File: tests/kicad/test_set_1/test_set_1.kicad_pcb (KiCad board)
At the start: 2 copper layers, 100 x 100 mm, 3 parts, among them J1 Vin, J2 Isens, J4 Conn_01x24_Socket

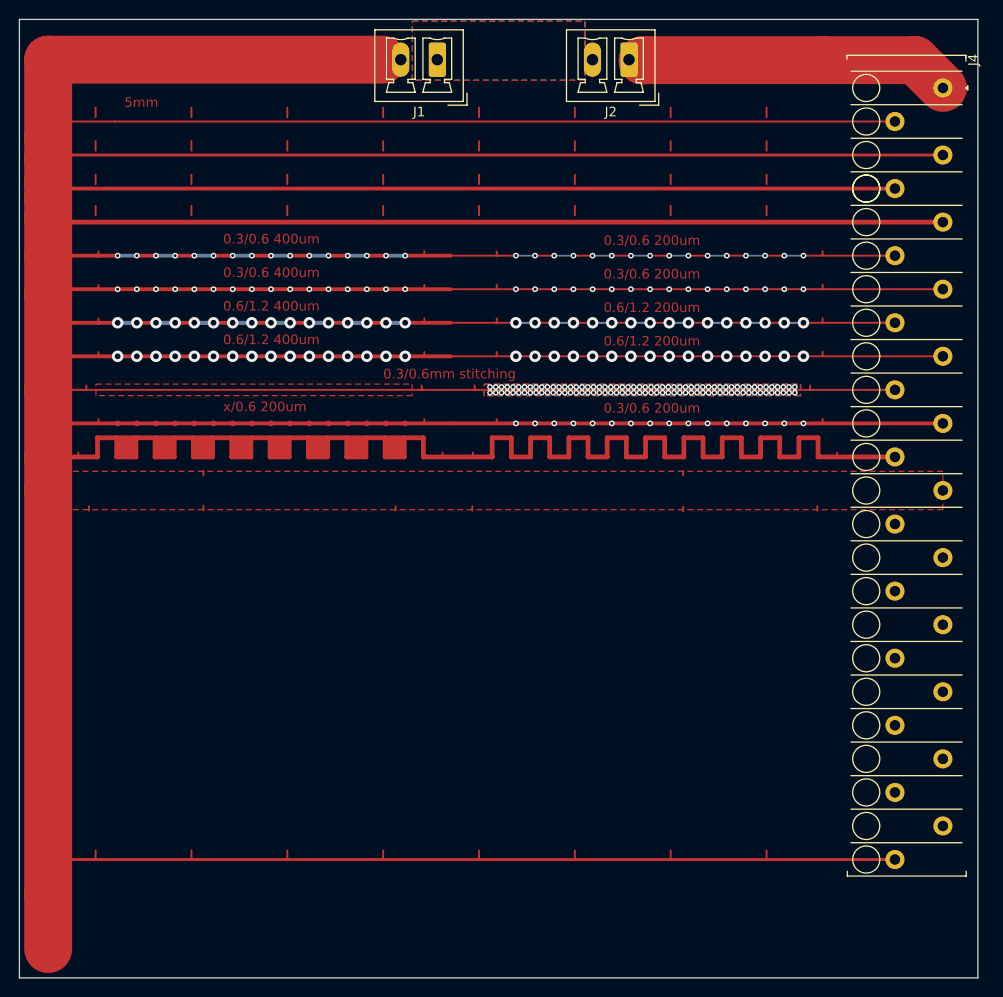
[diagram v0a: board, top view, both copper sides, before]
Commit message: test: More progress on the test_set_1 board
Add explicit test point pads to make test suite integration easier.
Also finish the "weird geometry" bunch of test cases.
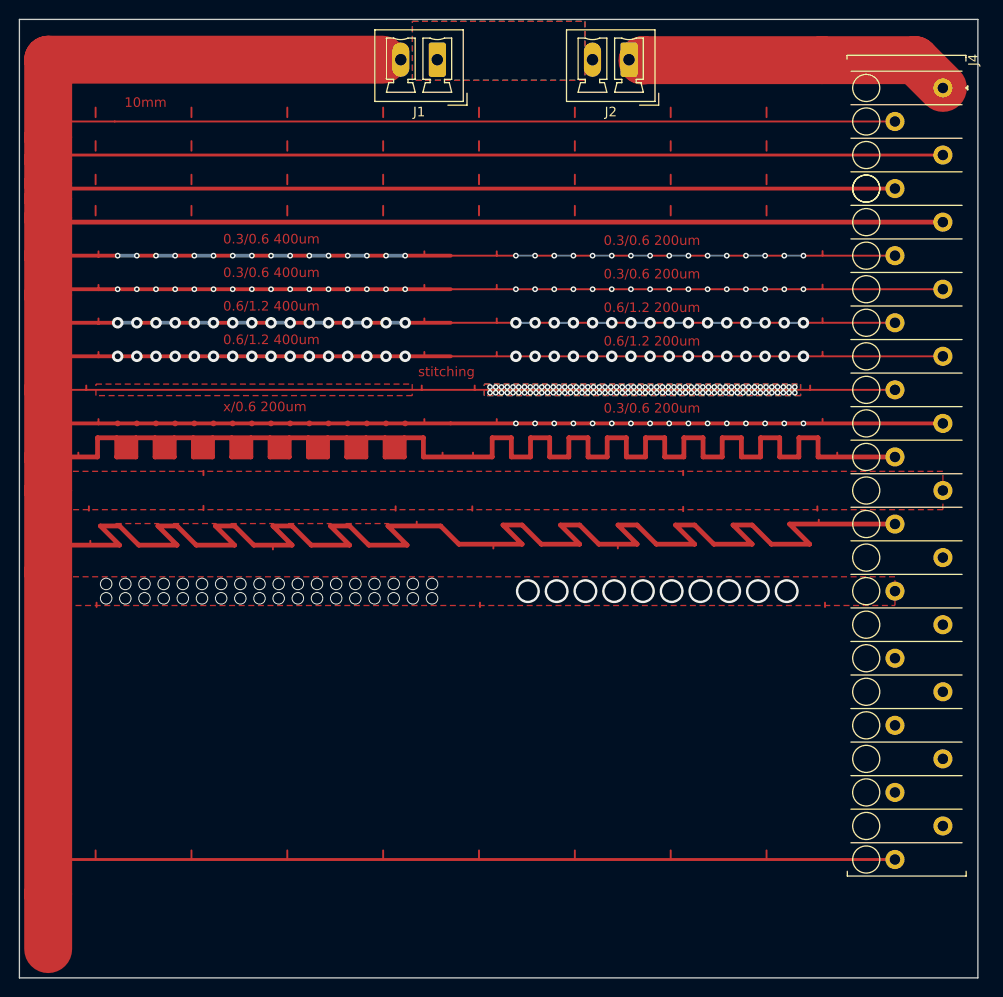
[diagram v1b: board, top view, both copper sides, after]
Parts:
- added TP1: TestPoint_Small, padne_footprints:ProbePoint, F.Cu at (107.2, 101.2)
- added TP10: TestPoint_Small, padne_footprints:ProbePoint, F.Cu at (144.2, 95.2)
- added TP11: TestPoint_Small, padne_footprints:ProbePoint, F.Cu at (147.3, 95.2)
- added TP12: TestPoint_Small, padne_footprints:ProbePoint, F.Cu at (185.3, 95.2)
- added TP13: TestPoint_Small, padne_footprints:ProbePoint, F.Cu at (108.2, 91.7)
- added TP14: TestPoint_Small, padne_footprints:ProbePoint, F.Cu at (142.2, 91.7)
- added TP15: TestPoint_Small, padne_footprints:ProbePoint, F.Cu at (149.8, 91.7)
- added TP16: TestPoint_Small, padne_footprints:ProbePoint, F.Cu at (183.8, 91.7)
- added TP17: TestPoint_Small, padne_footprints:ProbePoint, F.Cu at (107.0, 88.2)
- added TP18: TestPoint_Small, padne_footprints:ProbePoint, F.Cu at (142.0, 88.2)
- added TP19: TestPoint_Small, padne_footprints:ProbePoint, F.Cu at (147.5, 88.2)
- added TP2: TestPoint_Small, padne_footprints:ProbePoint, F.Cu at (119.2, 101.2)
- added TP20: TestPoint_Small, padne_footprints:ProbePoint, F.Cu at (182.5, 88.2)
- added TP21: TestPoint_Small, padne_footprints:ProbePoint, F.Cu at (108.2, 84.7)
- added TP22: TestPoint_Small, padne_footprints:ProbePoint, F.Cu at (142.2, 84.7)
- added TP23: TestPoint_Small, padne_footprints:ProbePoint, F.Cu at (149.8, 84.7)
- added TP24: TestPoint_Small, padne_footprints:ProbePoint, F.Cu at (183.8, 84.7)
- added TP25: TestPoint_Small, padne_footprints:ProbePoint, F.Cu at (108.2, 81.2)
- added TP26: TestPoint_Small, padne_footprints:ProbePoint, F.Cu at (142.2, 81.2)
- added TP27: TestPoint_Small, padne_footprints:ProbePoint, F.Cu at (149.8, 81.2)
- added TP28: TestPoint_Small, padne_footprints:ProbePoint, F.Cu at (183.8, 81.2)
- added TP29: TestPoint_Small, padne_footprints:ProbePoint, F.Cu at (108.2, 77.7)
- added TP3: TestPoint_Small, padne_footprints:ProbePoint, F.Cu at (119.2, 97.1)
- added TP30: TestPoint_Small, padne_footprints:ProbePoint, F.Cu at (142.2, 77.7)
- added TP31: TestPoint_Small, padne_footprints:ProbePoint, F.Cu at (149.8, 77.7)
- added TP32: TestPoint_Small, padne_footprints:ProbePoint, F.Cu at (183.8, 77.7)
- added TP33: TestPoint_Small, padne_footprints:ProbePoint, F.Cu at (108.2, 74.2)
- added TP34: TestPoint_Small, padne_footprints:ProbePoint, F.Cu at (142.2, 74.2)
- added TP35: TestPoint_Small, padne_footprints:ProbePoint, F.Cu at (149.8, 74.2)
- added TP36: TestPoint_Small, padne_footprints:ProbePoint, F.Cu at (183.8, 74.2)
- added TP37: TestPoint_Small, padne_footprints:ProbePoint, F.Cu at (107.4, 104.4)
- added TP38: TestPoint_Small, padne_footprints:ProbePoint, F.Cu at (141.4, 102.4)
- added TP39: TestPoint_Small, padne_footprints:ProbePoint, F.Cu at (149.4, 105.2)
- added TP4: TestPoint_Small, padne_footprints:ProbePoint, F.Cu at (139.2, 101.2)
- added TP40: TestPoint_Small, padne_footprints:ProbePoint, F.Cu at (183.4, 102.2)
- added TP41: TestPoint_Small, padne_footprints:ProbePoint, F.Cu at (126.5, 105.3)
- added TP42: TestPoint_Small, padne_footprints:ProbePoint, F.Cu at (162.4, 105.2)
- added TP43: TestPoint_Small, padne_footprints:ProbePoint, F.Cu at (108.0, 111.3)
- added TP44: TestPoint_Small, padne_footprints:ProbePoint, F.Cu at (148.1, 111.3)
- added TP45: TestPoint_Small, padne_footprints:ProbePoint, F.Cu at (184.1, 111.3)
- added TP5: TestPoint_Small, padne_footprints:ProbePoint, F.Cu at (147.2, 101.2)
- added TP6: TestPoint_Small, padne_footprints:ProbePoint, F.Cu at (169.2, 97.1)
- added TP7: TestPoint_Small, padne_footprints:ProbePoint, F.Cu at (169.2, 101.3)
- added TP8: TestPoint_Small, padne_footprints:ProbePoint, F.Cu at (183.2, 101.2)
- added TP9: TestPoint_Small, padne_footprints:ProbePoint, F.Cu at (106.2, 95.2)
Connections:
- J4 pad 14: unconnected-(J4-Pin_14-Pad14) -> GND
- J4 pad 16: unconnected-(J4-Pin_16-Pad16) -> GND
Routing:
- net GND: track 1288.3 -> 1443.0 mm, vias 252 -> 298
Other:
- board text added: "10mm"
- board text added: "stitching"
- board text removed: "0.3/0.6mm stitching"
- board text removed: "5mm"

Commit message: test: test_set_1 board almost finished
Gonna sleep on it a bit and then yolo order it.
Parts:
- added R1: 5u, Resistor_SMD:R_1206_3216Metric, F.Cu at (178.8, 113.2)
- added R10: 5u, Resistor_SMD:R_1206_3216Metric, F.Cu at (178.8, 116.7)
- added R11: 5u, Resistor_SMD:R_1206_3216Metric, F.Cu at (170.3, 116.7)
- added R12: 5u, Resistor_SMD:R_1206_3216Metric, F.Cu at (161.8, 116.7)
- added R13: 5u, Resistor_SMD:R_1206_3216Metric, F.Cu at (153.2, 116.7)
- added R14: 5u, Resistor_SMD:R_1206_3216Metric, F.Cu at (144.7, 116.7)
- added R15: 5u, Resistor_SMD:R_1206_3216Metric, F.Cu at (136.1, 116.7)
- added R16: 5u, Resistor_SMD:R_1206_3216Metric, F.Cu at (127.5, 116.7)
- added R17: 5u, Resistor_SMD:R_1206_3216Metric, F.Cu at (119.0, 116.7)
- added R18: 5u, Resistor_SMD:R_1206_3216Metric, F.Cu at (110.5, 116.7)
- added R19: 5u, Resistor_SMD:R_2512_6332Metric, F.Cu at (177.3, 120.2)
- added R2: 5u, Resistor_SMD:R_1206_3216Metric, F.Cu at (170.3, 113.2)
- added R20: 5u, Resistor_SMD:R_0805_2012Metric, F.Cu at (177.2, 125.0)
- added R21: 5u, Resistor_SMD:R_2512_6332Metric, F.Cu at (167.3, 120.2)
- added R22: 5u, Resistor_SMD:R_0805_2012Metric, F.Cu at (169.2, 125.0)
- added R23: 5u, Resistor_SMD:R_2512_6332Metric, F.Cu at (157.3, 120.2)
- added R24: 5u, Resistor_SMD:R_0805_2012Metric, F.Cu at (161.2, 125.0)
- added R25: 5u, Resistor_SMD:R_2512_6332Metric, F.Cu at (147.3, 120.2)
- added R26: 5u, Resistor_SMD:R_0805_2012Metric, F.Cu at (153.2, 125.0)
- added R27: 5u, Resistor_SMD:R_2512_6332Metric, F.Cu at (137.3, 120.2)
- added R28: 5u, Resistor_SMD:R_0805_2012Metric, F.Cu at (145.2, 125.0)
- added R29: 5u, Resistor_SMD:R_2512_6332Metric, F.Cu at (127.3, 120.2)
- added R3: 5u, Resistor_SMD:R_1206_3216Metric, F.Cu at (161.8, 113.2)
- added R30: 5u, Resistor_SMD:R_0805_2012Metric, F.Cu at (137.2, 125.0)
- added R31: 5u, Resistor_SMD:R_2512_6332Metric, F.Cu at (117.3, 120.2)
- added R32: 5u, Resistor_SMD:R_0805_2012Metric, F.Cu at (129.2, 125.0)
- added R33: 5u, Resistor_SMD:R_0805_2012Metric, F.Cu at (121.2, 125.0)
- added R34: 5u, Resistor_SMD:R_0805_2012Metric, F.Cu at (113.2, 125.0)
- added R35: 5u, Resistor_SMD:R_0805_2012Metric, F.Cu at (177.2, 128.6)
- added R36: 5u, Resistor_SMD:R_0805_2012Metric, F.Cu at (169.2, 128.6)
- added R37: 5u, Resistor_SMD:R_0805_2012Metric, F.Cu at (161.2, 128.6)
- added R38: 5u, Resistor_SMD:R_0805_2012Metric, F.Cu at (153.2, 128.6)
- added R39: 5u, Resistor_SMD:R_0805_2012Metric, F.Cu at (145.2, 128.6)
- added R4: 5u, Resistor_SMD:R_1206_3216Metric, F.Cu at (153.2, 113.2)
- added R40: 5u, Resistor_SMD:R_0805_2012Metric, F.Cu at (137.2, 128.6)
- added R41: 5u, Resistor_SMD:R_0805_2012Metric, F.Cu at (129.2, 128.6)
- added R42: 5u, Resistor_SMD:R_0805_2012Metric, F.Cu at (121.2, 128.6)
- added R43: 5u, Resistor_SMD:R_0805_2012Metric, F.Cu at (113.2, 128.6)
- added R5: 5u, Resistor_SMD:R_1206_3216Metric, F.Cu at (144.7, 113.2)
- added R6: 5u, Resistor_SMD:R_1206_3216Metric, F.Cu at (136.1, 113.2)
- added R7: 5u, Resistor_SMD:R_1206_3216Metric, F.Cu at (127.5, 113.2)
- added R8: 5u, Resistor_SMD:R_1206_3216Metric, F.Cu at (119.0, 113.2)
- added R9: 5u, Resistor_SMD:R_1206_3216Metric, F.Cu at (110.5, 113.2)
- added SYM1: Logo_Open_Hardware_Large, Symbol:OSHW-Symbol_6.7x6mm_SilkScreen, F.Cu at (170.8, 54.0)
- added TP46: TestPoint_Small, padne_footprints:ProbePoint, F.Cu at (107.5, 112.7)
- added TP47: TestPoint_Small, padne_footprints:ProbePoint, F.Cu at (181.8, 112.7)
- added TP48: TestPoint_Small, padne_footprints:ProbePoint, F.Cu at (181.8, 116.0)
- added TP49: TestPoint_Small, padne_footprints:ProbePoint, F.Cu at (107.5, 116.0)
- added TP50: TestPoint_Small, padne_footprints:ProbePoint, F.Cu at (183.2, 124.6)
- added TP51: TestPoint_Small, padne_footprints:ProbePoint, F.Cu at (183.8, 119.8)
- added TP52: TestPoint_Small, padne_footprints:ProbePoint, F.Cu at (111.3, 119.7)
- added TP53: TestPoint_Small, padne_footprints:ProbePoint, F.Cu at (107.3, 124.6)
- added TP54: TestPoint_Small, padne_footprints:ProbePoint, F.Cu at (183.2, 128.2)
- added TP55: TestPoint_Small, padne_footprints:ProbePoint, F.Cu at (107.3, 128.2)
- added TP56: TestPoint_Small, padne_footprints:ProbePoint, F.Cu at (158.7, 128.6)
- added TP57: TestPoint_Small, padne_footprints:ProbePoint, F.Cu at (144.3, 123.5)
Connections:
- J4 pad 17: unconnected-(J4-Pin_17-Pad17) -> Net-(J4-Pin_17)
- J4 pad 18: unconnected-(J4-Pin_18-Pad18) -> Net-(J4-Pin_18)
- J4 pad 19: unconnected-(J4-Pin_19-Pad19) -> Net-(J4-Pin_19)
- J4 pad 20: unconnected-(J4-Pin_20-Pad20) -> Net-(J4-Pin_20)
- J4 pad 21: unconnected-(J4-Pin_21-Pad21) -> Net-(J4-Pin_21)
- J4 pad 23: unconnected-(J4-Pin_23-Pad23) -> GND
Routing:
- net +VDC: track 32.6 -> 0.00 mm
- net Net-(J4-Pin_21): track 0.00 -> 18.8 mm
- net Net-(J4-Pin_19): track 0.00 -> 16.1 mm
- net Net-(J4-Pin_17): track 0.00 -> 16.0 mm
- net Net-(J4-Pin_20): track 0.00 -> 13.8 mm
- net Net-(J4-Pin_18): track 0.00 -> 11.0 mm
- net Net-(R42-Pad1): track 0.00 -> 6.18 mm, vias 0 -> 2
- net Net-(R41-Pad2): track 0.00 -> 6.18 mm, vias 0 -> 2
- net Net-(R40-Pad1): track 0.00 -> 6.18 mm, vias 0 -> 2
- net Net-(R39-Pad2): track 0.00 -> 6.18 mm, vias 0 -> 2
- net Net-(R38-Pad2): track 0.00 -> 6.18 mm, vias 0 -> 2
- net Net-(R37-Pad2): track 0.00 -> 6.18 mm, vias 0 -> 2
- net Net-(R36-Pad2): track 0.00 -> 6.18 mm, vias 0 -> 2
- net Net-(R35-Pad2): track 0.00 -> 6.18 mm, vias 0 -> 2
- net Net-(R5-Pad2): track 0.00 -> 5.64 mm
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- added copper zone on F.Cu, net +VDC
- added copper zone on F.Cu, net Net-(R19-Pad2)
- added copper zone on F.Cu, net Net-(R20-Pad2)
- added copper zone on F.Cu, net Net-(R21-Pad2)
- added copper zone on F.Cu, net Net-(R22-Pad2)
- added copper zone on F.Cu, net Net-(R23-Pad2)
- added copper zone on F.Cu, net Net-(R24-Pad2)
- added copper zone on F.Cu, net Net-(R25-Pad2)
- added copper zone on F.Cu, net Net-(R26-Pad2)
- added copper zone on F.Cu, net Net-(R27-Pad2)
- added copper zone on F.Cu, net Net-(R28-Pad2)
- added copper zone on F.Cu, net Net-(R29-Pad1)
- added copper zone on F.Cu, net Net-(R30-Pad1)
- added copper zone on F.Cu, net Net-(R32-Pad2)
- added copper zone on F.Cu, net Net-(R33-Pad1)
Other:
- board size 100 x 100 mm -> 100 x 92 mm
- board text added: "200μm"
- board text added: "300μm"
- board text added: "400μm"
- board text added: "500μm"
- board text added: "A"
- board text added: "B"
- board text added: "CERN-OHL-S"
- board text added: "Supported by NLnet"
- board text added: "bubbles"
- board text added: "by Josef Gajdusek <atx@atx.name>"
- board text added: "corners"
- board text added: "github.com/atx/padne"
- board text added: "padne test_set_1"
- board text added: "zigzag"

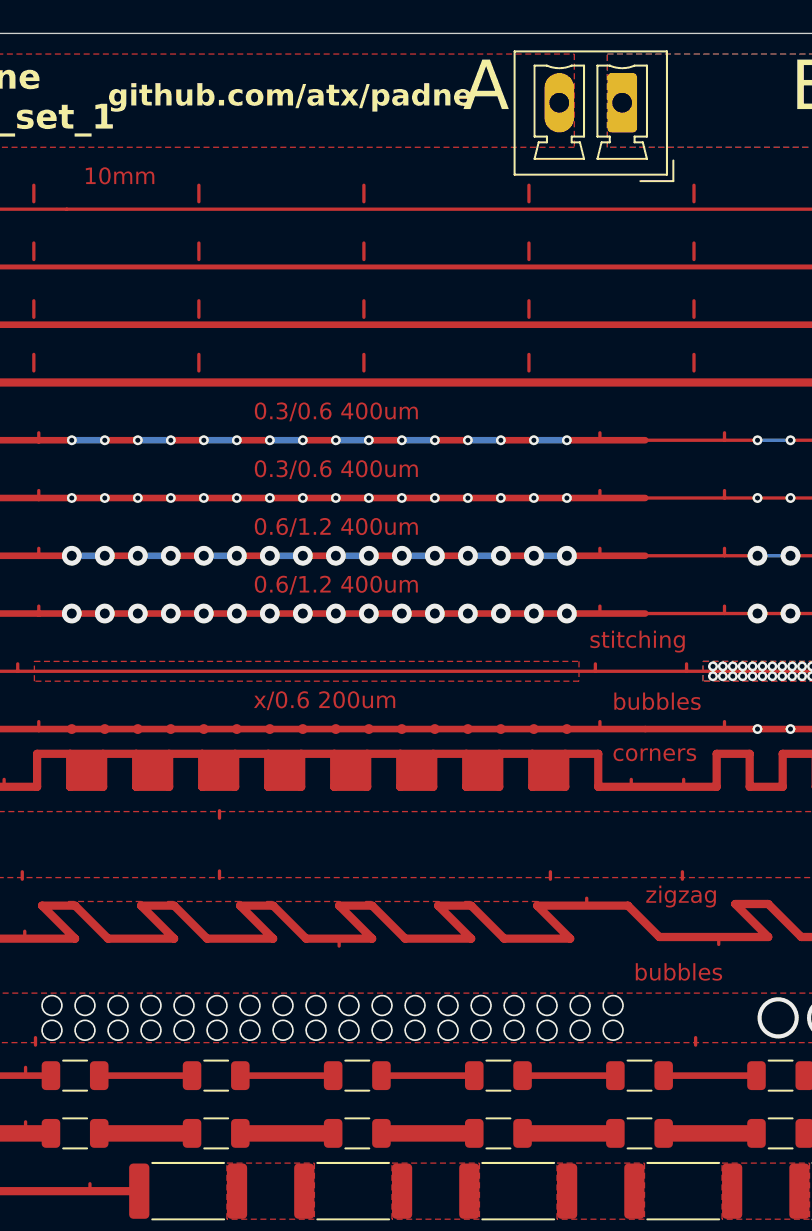
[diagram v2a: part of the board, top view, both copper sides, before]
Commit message: test: test_set_1 finishing touches (silkscreen and more test pads)
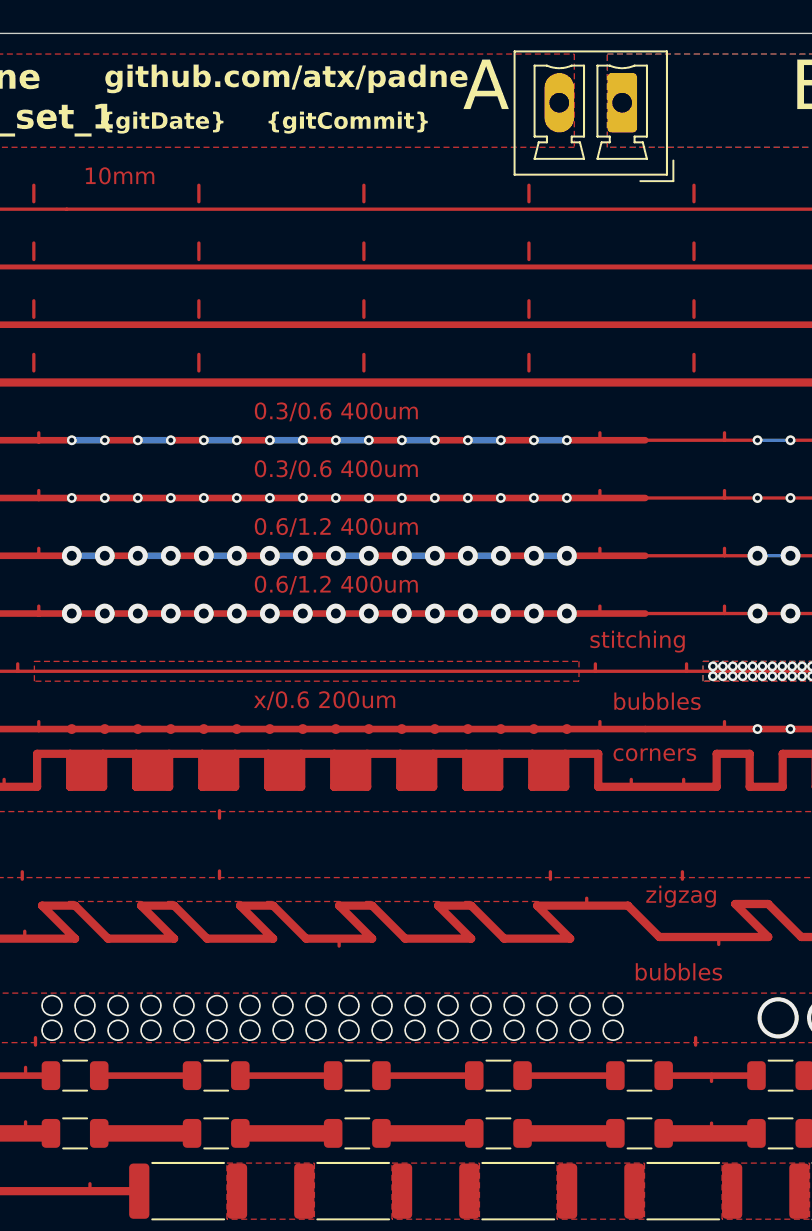
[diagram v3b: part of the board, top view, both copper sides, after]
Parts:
- added TP58: TestPoint_Small, padne_footprints:ProbePoint, F.Cu at (149.0, 116.0)
- added TP59: TestPoint_Small, padne_footprints:ProbePoint, F.Cu at (149.0, 113.5)
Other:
- board text added: "{gitCommit}"
- board text added: "{gitDate}"

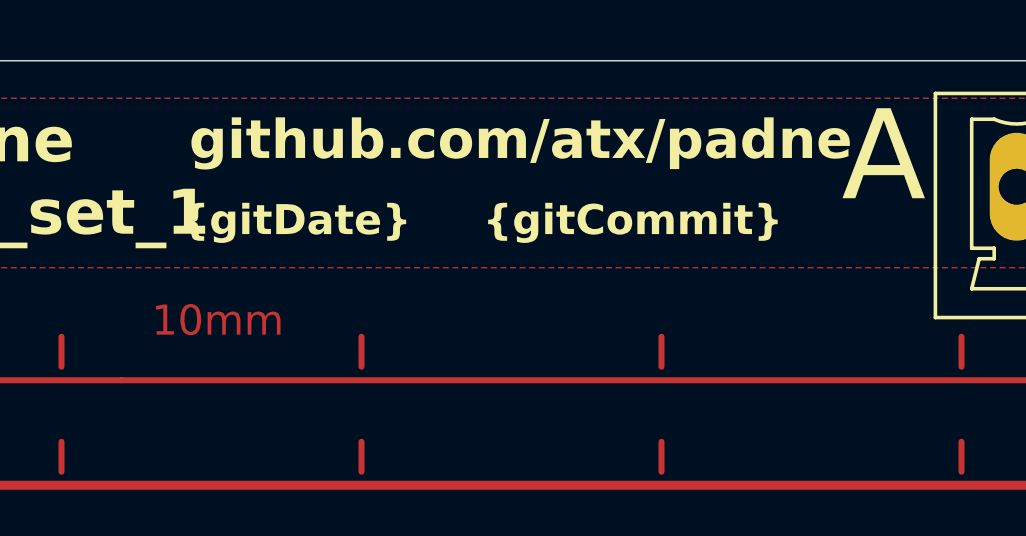
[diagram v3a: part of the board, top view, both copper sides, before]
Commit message: test: test_set_1 bake in date
Aisler eats raw .kicad_pcb files and I do not want to bother with force
feeding them JLCPCB-style gerbers.
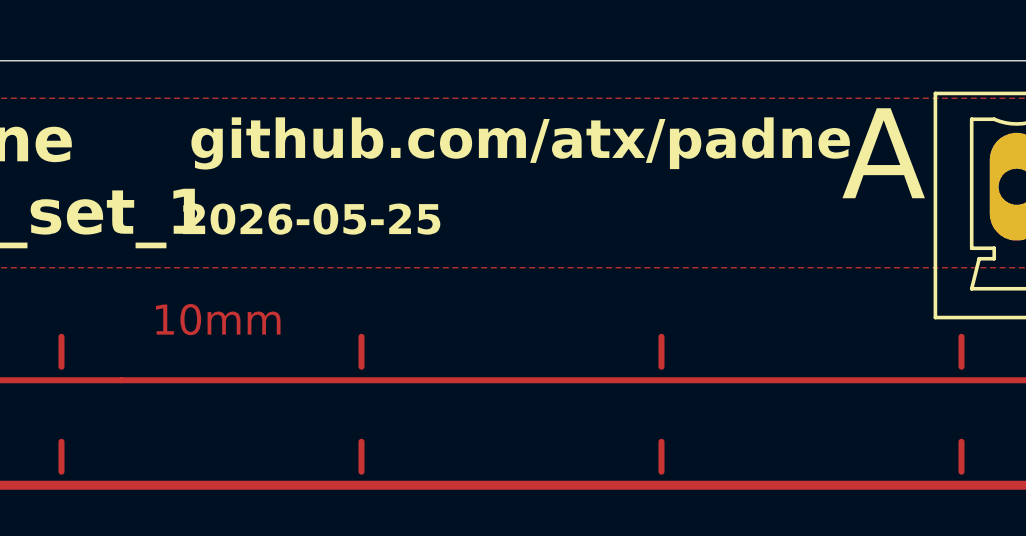
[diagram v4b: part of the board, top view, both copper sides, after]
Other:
- board text added: "2026-05-25"
- board text removed: "{gitCommit}"
- board text removed: "{gitDate}"
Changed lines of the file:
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@@
 		)
 	)
-	(gr_text "{gitDate}"
+	(gr_text "2026-05-25"
 		(at 111.9 55.9 0)
 		(layer "F.SilkS")
 		(effects
-			(font
-				(size 1 1)
-				(thickness 0.2)
-				(bold yes)
-			)
-			(justify left bottom)
-		)
-	)
-	(gr_text "{gitCommit}"
-		(at 122 55.9 0)
-		(layer "F.SilkS")
-		(effects

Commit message: test: Add probe points to test_set_1
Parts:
- added TP60: TestPoint_Small, padne_footprints:ProbePoint, F.Cu at (108.0, 60.6)
- added TP61: TestPoint_Small, padne_footprints:ProbePoint, F.Cu at (177.9, 60.6)
- added TP62: TestPoint_Small, padne_footprints:ProbePoint, F.Cu at (108.0, 64.2)
- added TP63: TestPoint_Small, padne_footprints:ProbePoint, F.Cu at (177.9, 64.2)
- added TP64: TestPoint_Small, padne_footprints:ProbePoint, F.Cu at (108.0, 67.7)
- added TP65: TestPoint_Small, padne_footprints:ProbePoint, F.Cu at (177.9, 67.7)
- added TP66: TestPoint_Small, padne_footprints:ProbePoint, F.Cu at (108.0, 71.2)
- added TP67: TestPoint_Small, padne_footprints:ProbePoint, F.Cu at (177.9, 71.2)

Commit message: test(test_set_1): Match sim parameters to real PCB
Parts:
- TP1, TP10, TP11, TP12, TP13, TP14, TP15, TP16, TP17, TP18, TP19, TP2, TP20, TP21, TP22, TP23, TP24, TP25, TP26, TP27, TP28, TP29, TP3, TP30, TP31, TP32, TP33, TP34, TP35, TP36, TP37, TP38, TP39, TP4, TP40, TP41, TP42, TP43, TP44, TP45, TP46, TP47, TP48, TP49, TP5, TP50, TP51, TP52, TP53, TP54, TP55, TP56, TP57, TP58, TP59, TP6, TP60, TP61, TP62, TP63, TP64, TP65, TP66, TP67, TP7, TP8, TP9: value TestPoint_Small -> ~
